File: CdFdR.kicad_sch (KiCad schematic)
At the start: 17 parts, among them J1 Moteur_1, J2 Moteur_2, J3 Moteur_3, J4 Moteur_4, U1 ESP32-S3-N16R8-DEVBOARD

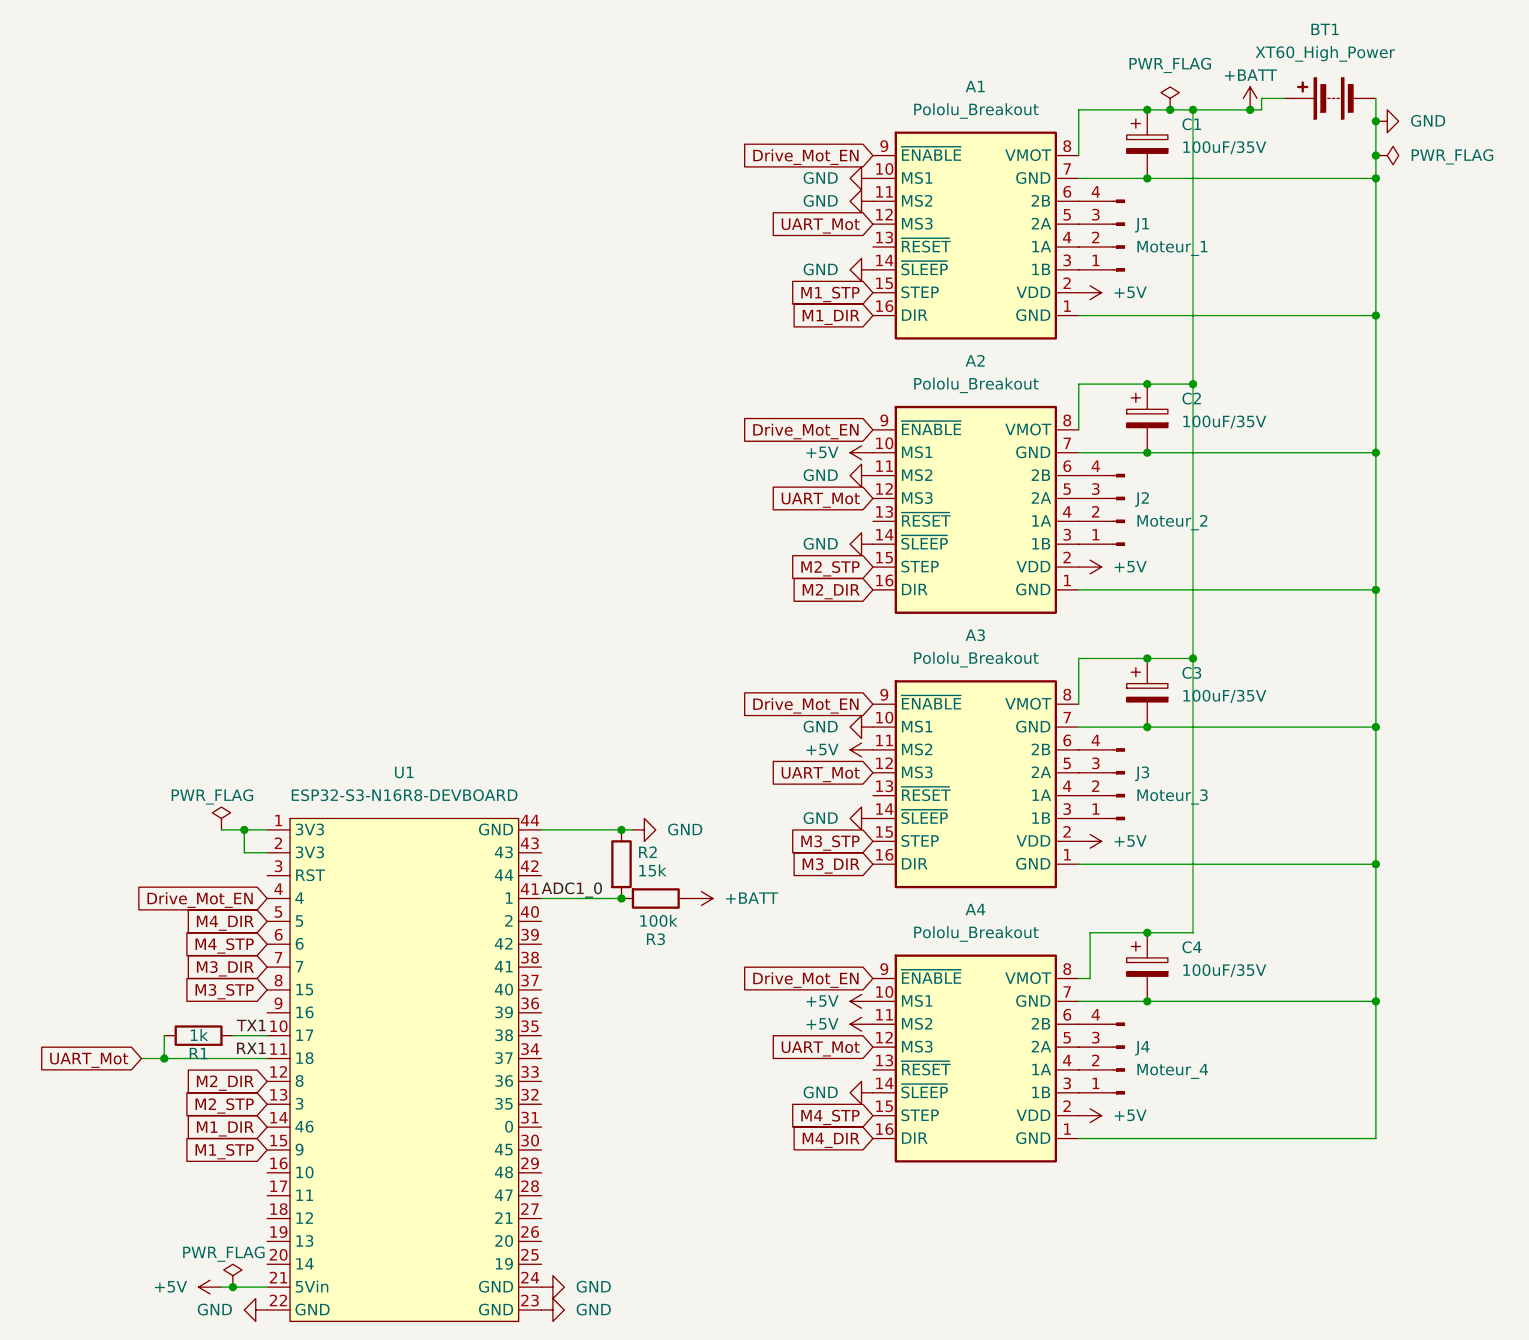
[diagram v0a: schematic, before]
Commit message: Changed drivers uart code due to error on hand soldered board
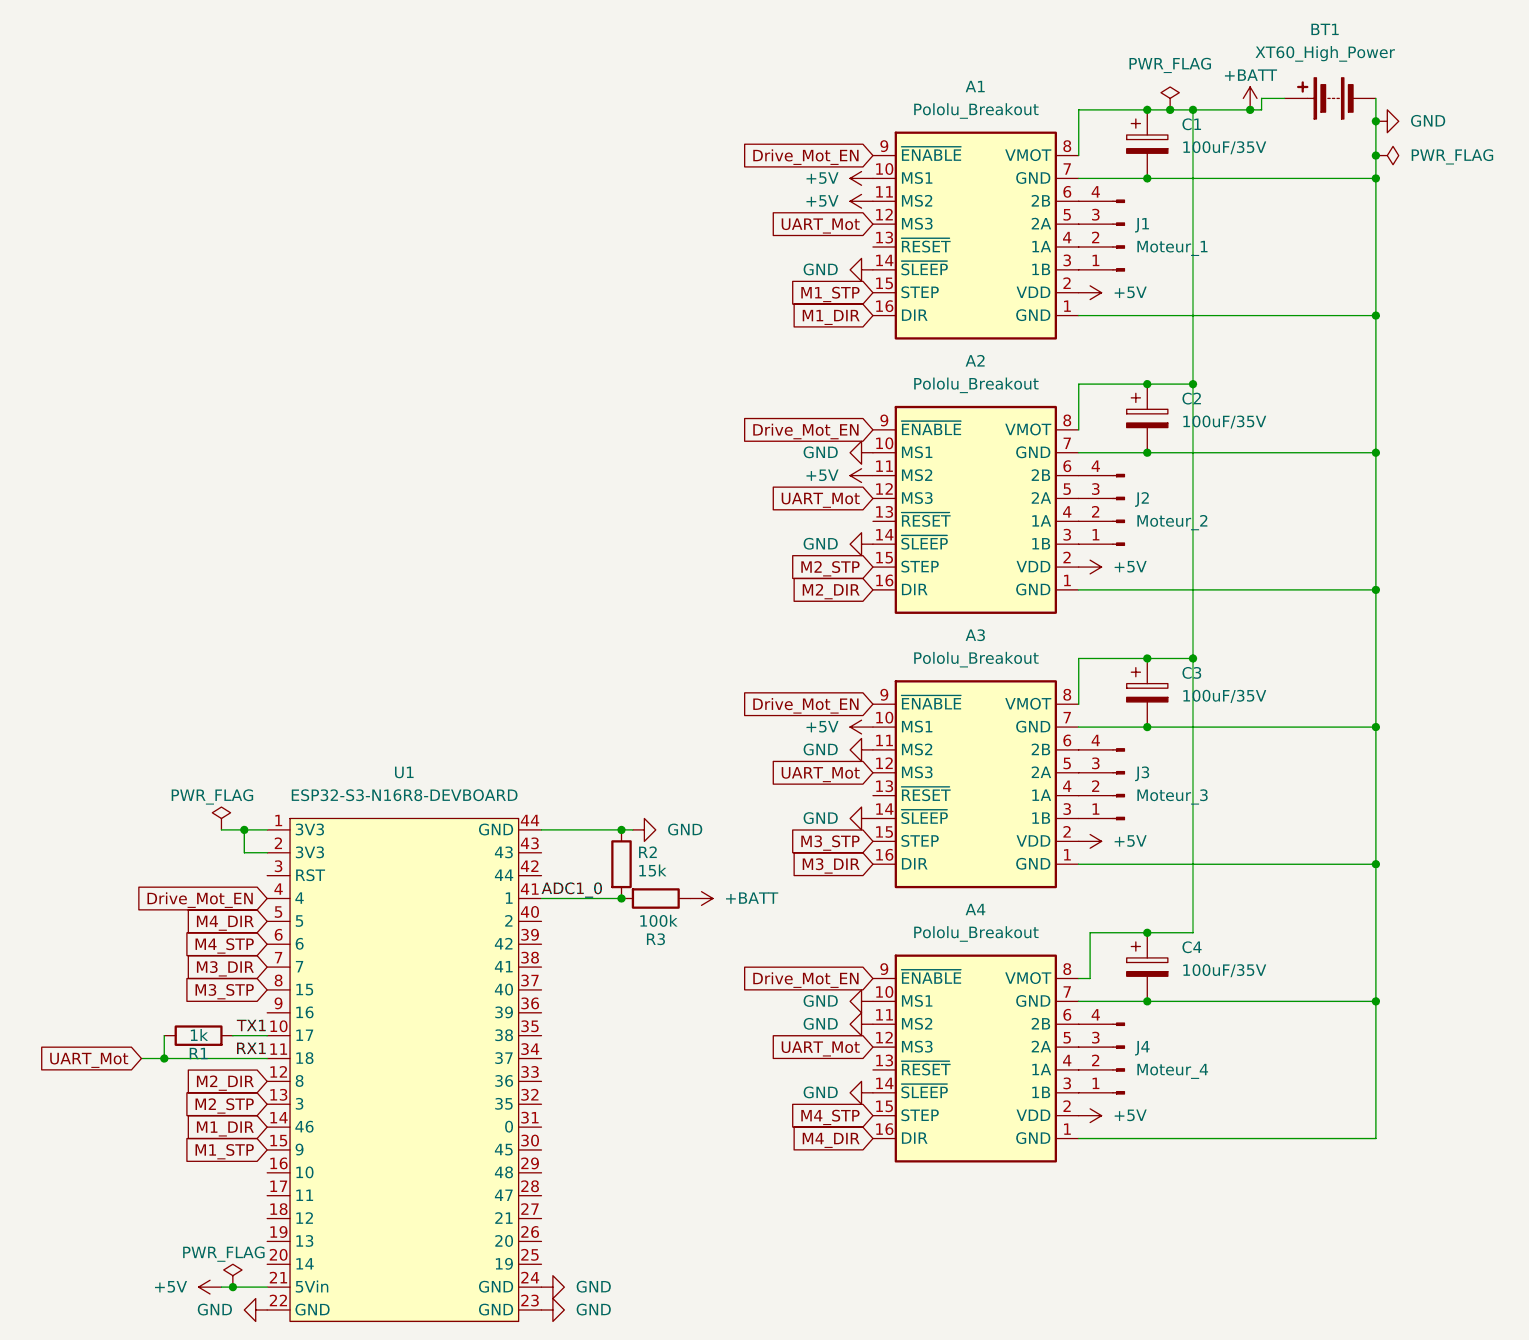
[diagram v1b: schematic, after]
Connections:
- net +5V: now also A1.10 (MS1), A1.11 (MS2), A2.11 (MS2), A3.10 (MS1); no longer A2.10 (MS1), A3.11 (MS2), A4.10 (MS1), A4.11 (MS2)
- net GND: now also A2.10 (MS1), A3.11 (MS2), A4.10 (MS1), A4.11 (MS2); no longer A1.10 (MS1), A1.11 (MS2), A2.11 (MS2), A3.10 (MS1)

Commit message: Correction des pins des moteurs pour être en accord avec carte soudé
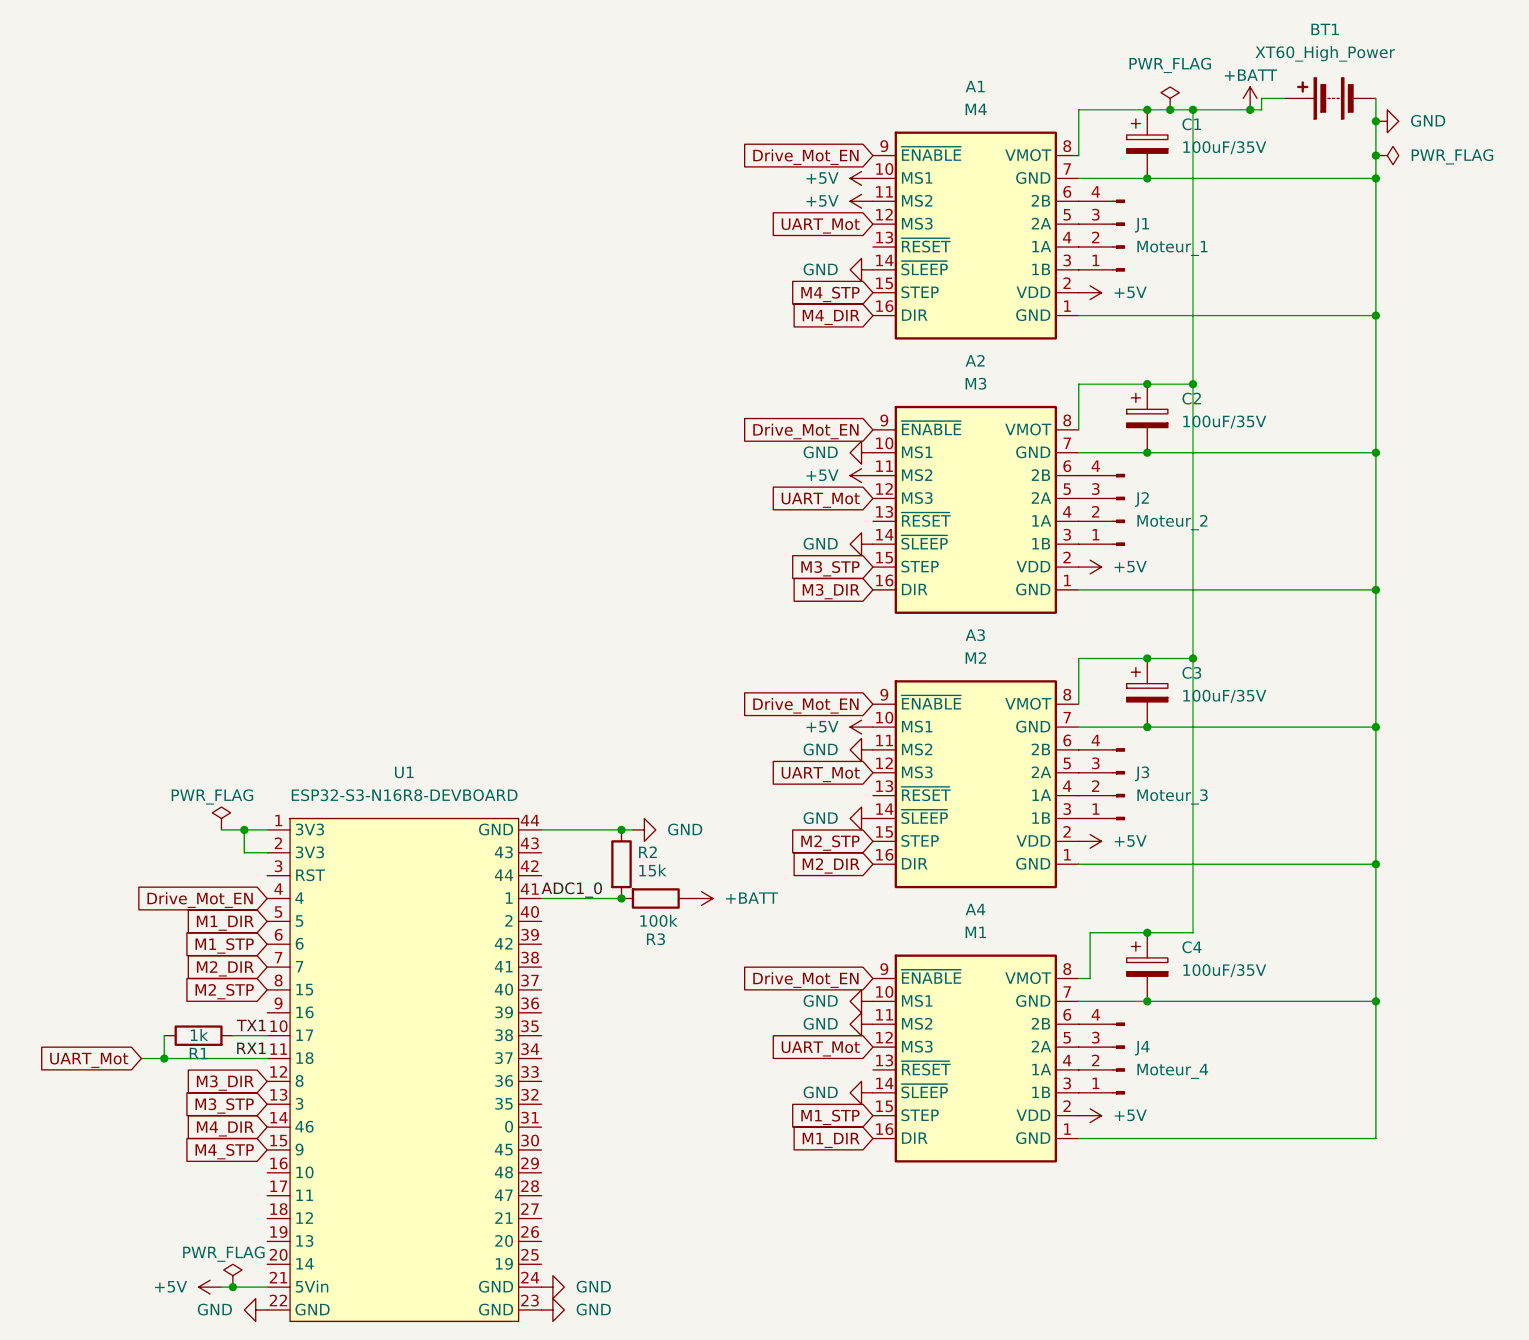
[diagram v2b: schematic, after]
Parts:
- A1: value Pololu_Breakout -> M4
- A2: value Pololu_Breakout -> M3
- A3: value Pololu_Breakout -> M2
- A4: value Pololu_Breakout -> M1
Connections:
- net M1_DIR: now also A4.16 (DIR), U1.5; no longer A1.16 (DIR), U1.14 (46)
- net M1_STP: now also A4.15 (STEP), U1.6; no longer A1.15 (STEP), U1.15 (9)
- net M2_DIR: now also A3.16 (DIR), U1.7; no longer A2.16 (DIR), U1.12 (8)
- net M2_STP: now also A3.15 (STEP), U1.8 (15); no longer A2.15 (STEP), U1.13 (3)
- net M3_DIR: now also A2.16 (DIR), U1.12 (8); no longer A3.16 (DIR), U1.7
- net M3_STP: now also A2.15 (STEP), U1.13 (3); no longer A3.15 (STEP), U1.8 (15)
- net M4_DIR: now also A1.16 (DIR), U1.14 (46); no longer A4.16 (DIR), U1.5
- net M4_STP: now also A1.15 (STEP), U1.15 (9); no longer A4.15 (STEP), U1.6
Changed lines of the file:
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@@
 		)
 	)
-	(global_label "M1_DIR"
+	(global_label "M4_DIR"
 		(shape input)
 		(at 43.18 162.56 180)
@@
 		)
 	)
-	(global_label "M2_DIR"
+	(global_label "M3_DIR"
 		(shape input)
 		(at 43.18 157.48 180)
@@
 		)
 	)
-	(global_label "M2_DIR"
+	(global_label "M3_DIR"
 		(shape input)
 		(at 110.49 102.87 180)
@@
 		)
 	)
-	(global_label "M3_STP"
+	(global_label "M2_STP"
 		(shape input)
 		(at 110.49 130.81 180)
@@
 		)
 	)
-	(global_label "M1_STP"
+	(global_label "M4_STP"
 		(shape input)
 		(at 110.49 69.85 180)
@@
 		)
 	)
-	(global_label "M2_STP"
+	(global_label "M3_STP"
 		(shape input)
 		(at 110.49 100.33 180)
@@
 		)
 	)
-	(global_label "M4_STP"
+	(global_label "M1_STP"
 		(shape input)
 		(at 43.18 142.24 180)
@@
 		)
 	)
-	(global_label "M4_DIR"
+	(global_label "M1_DIR"
 		(shape input)
 		(at 43.18 139.7 180)
@@
 		)
 	)
-	(global_label "M1_STP"
+	(global_label "M4_STP"
 		(shape input)
 		(at 43.18 165.1 180)
@@
 		)
 	)
-	(global_label "M4_STP"
+	(global_label "M1_STP"
 		(shape input)
 		(at 110.49 161.29 180)
@@
 		)
 	)
-	(global_label "M3_DIR"
+	(global_label "M2_DIR"
 		(shape input)
 		(at 110.49 133.35 180)
@@
 		)
 	)
-	(global_label "M4_DIR"
+	(global_label "M1_DIR"
 		(shape input)
 		(at 110.49 163.83 180)
@@
 		)
 	)
-	(global_label "M3_STP"
+	(global_label "M2_STP"
 		(shape input)
 		(at 43.18 147.32 180)
@@
 		)
 	)
-	(global_label "M1_DIR"
+	(global_label "M4_DIR"
 		(shape input)
 		(at 110.49 72.39 180)
@@
 		)
 	)
-	(global_label "M3_DIR"
+	(global_label "M2_DIR"
 		(shape input)
 		(at 43.18 144.78 180)
@@
 		)
 	)
-	(global_label "M2_STP"
+	(global_label "M3_STP"
 		(shape input)
 		(at 43.18 160.02 180)
@@
 		(dnp no)
 		(fields_autoplaced yes)
-		(property "Reference" "#PWR017"
+		(property "Reference" "#PWR07"
 			(at 114.3 57.15 0)
 			(effects
@@
 			(project "CdFdR"
 				(path "/f91e69f4-9fec-420d-9fad-eb44c074ac19"
-					(reference "#PWR017")
+					(reference "#PWR07")
 					(unit 1)
 				)
@@
 		(dnp no)
 		(fields_autoplaced yes)
-		(property "Reference" "#PWR014"
+		(property "Reference" "#PWR013"
 			(at 114.3 118.11 0)
 			(effects
@@
 			(project "CdFdR"
 				(path "/f91e69f4-9fec-420d-9fad-eb44c074ac19"
-					(reference "#PWR014")
+					(reference "#PWR013")
 					(unit 1)
 				)
@@
 			)
 		)
-		(property "Value" "Pololu_Breakout"
+		(property "Value" "M1"
 			(at 121.92 140.97 0)
 			(effects
@@
 		(dnp no)
 		(fields_autoplaced yes)
-		(property "Reference" "#PWR011"
+		(property "Reference" "#PWR010"
 			(at 104.14 87.63 0)
 			(effects
@@
 			(project "CdFdR"
 				(path "/f91e69f4-9fec-420d-9fad-eb44c074ac19"
-					(reference "#PWR011")
+					(reference "#PWR010")
 					(unit 1)
 				)
@@
 			)
 		)
-		(property "Value" "Pololu_Breakout"
+		(property "Value" "M4"
 			(at 121.92 49.53 0)
 			(effects
@@
 			)
 		)
-		(property "Value" "Pololu_Breakout"
+		(property "Value" "M3"
 			(at 121.92 80.01 0)
 			(effects
@@
 			)
 		)
-		(property "Value" "Pololu_Breakout"
+		(property "Value" "M2"
 			(at 121.92 110.49 0)
 			(effects
@@
 		(dnp no)
 		(fields_autoplaced yes)
-		(property "Reference" "#PWR016"
+		(property "Reference" "#PWR017"
 			(at 104.14 151.13 0)
 			(effects
@@
 			(project "CdFdR"
 				(path "/f91e69f4-9fec-420d-9fad-eb44c074ac19"
-					(reference "#PWR016")
+					(reference "#PWR017")
 					(unit 1)
 				)
@@
 		(dnp no)
 		(fields_autoplaced yes)
-		(property "Reference" "#PWR010"
+		(property "Reference" "#PWR011"
 			(at 114.3 90.17 0)
 			(effects
@@
 			(project "CdFdR"
 				(path "/f91e69f4-9fec-420d-9fad-eb44c074ac19"
-					(reference "#PWR010")
+					(reference "#PWR011")
 					(unit 1)
 				)
@@
 		(dnp no)
 		(fields_autoplaced yes)
-		(property "Reference" "#PWR025"
+		(property "Reference" "#PWR016"
 			(at 104.14 148.59 0)
 			(effects
@@
 			(project "CdFdR"
 				(path "/f91e69f4-9fec-420d-9fad-eb44c074ac19"
-					(reference "#PWR025")
+					(reference "#PWR016")
 					(unit 1)
 				)
@@
 		(dnp no)
 		(fields_autoplaced yes)
-		(property "Reference" "#PWR013"
+		(property "Reference" "#PWR014"
 			(at 104.14 120.65 0)
 			(effects
@@
 			(project "CdFdR"
 				(path "/f91e69f4-9fec-420d-9fad-eb44c074ac19"
-					(reference "#PWR013")
+					(reference "#PWR014")
 					(unit 1)
 				)
@@
 		(dnp no)
 		(fields_autoplaced yes)
-		(property "Reference" "#PWR07"
+		(property "Reference" "#PWR08"
 			(at 114.3 59.69 0)
 			(effects
@@
 			(project "CdFdR"
 				(path "/f91e69f4-9fec-420d-9fad-eb44c074ac19"
-					(reference "#PWR07")
+					(reference "#PWR08")
 					(unit 1)
 				)
